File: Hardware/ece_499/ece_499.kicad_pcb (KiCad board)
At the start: 2 copper layers, 110.8 x 70 mm, 64 parts, among them J1 Conn_01x04, J2 Conn_01x04, J3 Conn_01x04, J4 Conn_01x04, J5 Conn_01x04, Q1 DMN2004WK, Q2 DMN2004WK, Q3 DMN2004WK, Q4 DMN2004WK, SW1 Encoder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

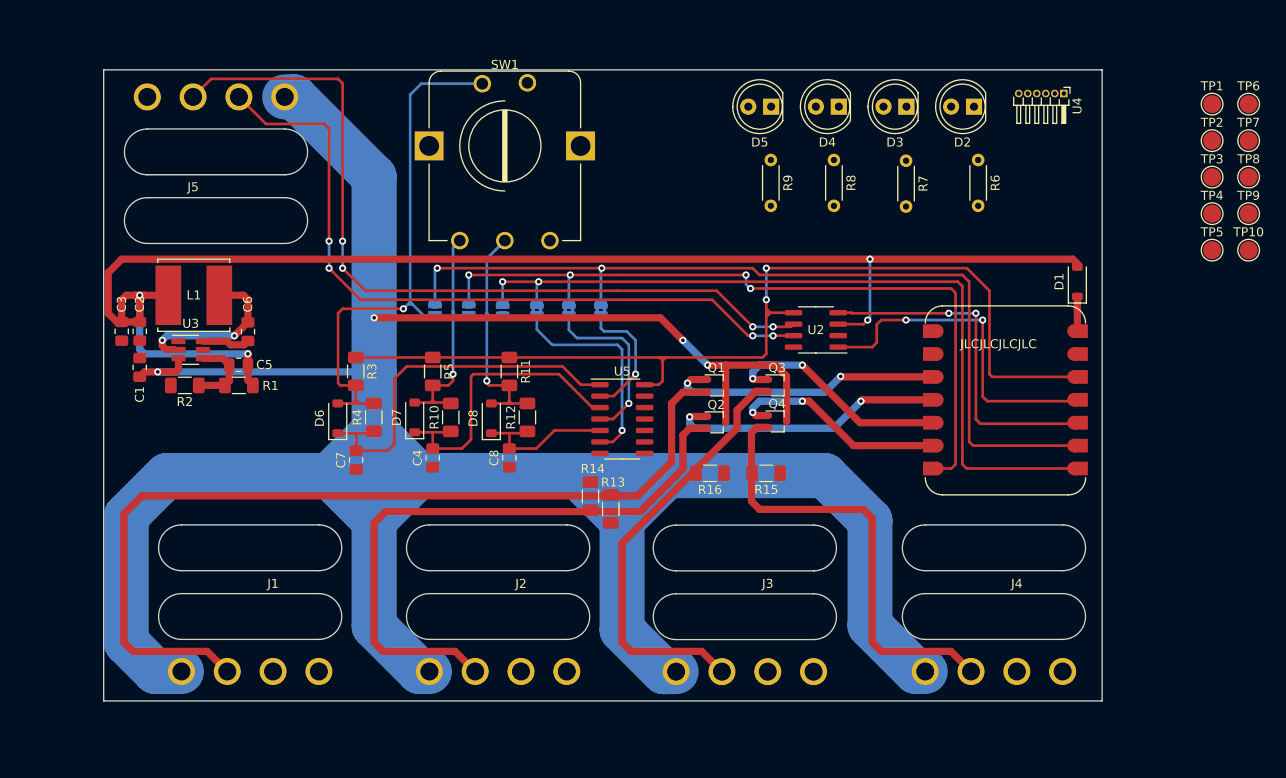
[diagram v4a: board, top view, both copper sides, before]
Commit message: Ground plane and start stitching vias
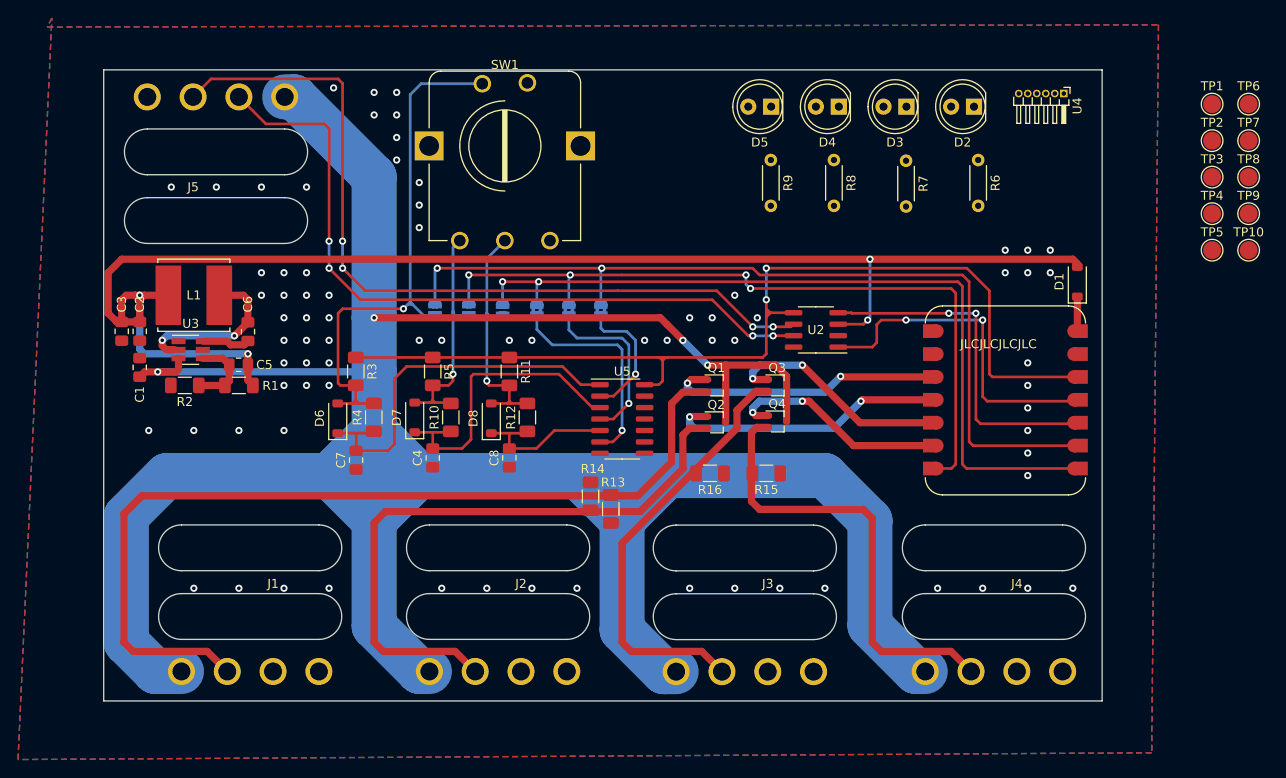
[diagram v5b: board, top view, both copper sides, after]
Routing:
- net GND: vias 0 -> 77
- added copper zone on B.Cu, net GND
- added copper zone on F.Cu, net GND
